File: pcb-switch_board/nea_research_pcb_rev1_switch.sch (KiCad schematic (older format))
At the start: 8 parts, among them P1 CONN_02X15, P2 CONN_02X13, P3 CONN_02X30, U1 QS4A110, U2 QS4A110, U3 QS4A110, U4 QS4A110, U5 QS4A110

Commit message: -progress on switch board layout
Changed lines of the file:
@@
 Text Label 1655 4540 0    60   ~ 0
 N2
-Text Label 1635 5300 0    60   ~ 0
+Text Label 1625 5460 0    60   ~ 0
 O2
-Text Label 1635 5460 0    60   ~ 0
+Text Label 1630 5300 0    60   ~ 0
 P2
 Text Label 1635 5660 0    60   ~ 0
@@
 Text Label 1605 6850 0    60   ~ 0
 U2
-Text Label 1590 7050 0    60   ~ 0
+Text Label 1610 7370 0    60   ~ 0
 V2
 Text Label 1570 1235 0    60   ~ 0
 MID2
-Text Label 1660 4100 0    60   ~ 0
+Text Label 1635 3780 0    60   ~ 0
 L1
 Text Label 1660 4300 0    60   ~ 0
@@
 Text Label 1655 4460 0    60   ~ 0
 N1
-Text Label 1640 5220 0    60   ~ 0
+Text Label 1630 5540 0    60   ~ 0
 O1
-Text Label 1640 5380 0    60   ~ 0
+Text Label 1630 5380 0    60   ~ 0
 P1
-Text Label 1640 5540 0    60   ~ 0
+Text Label 1625 5220 0    60   ~ 0
 Q1
 Text Label 1640 5740 0    60   ~ 0
@@
 Text Label 1610 6930 0    60   ~ 0
 V1
-Text Label 1545 7370 0    60   ~ 0
+Text Label 1530 7050 0    60   ~ 0
 SCL
+Text Label 1535 7130 0    60   ~ 0
+SDA
 Text Label 1535 7290 0    60   ~ 0
-SDA
-Text Label 1540 7130 0    60   ~ 0
 LED1
-Text Label 1520 7210 0    60   ~ 0
+Text Label 1535 7210 0    60   ~ 0
 LED2
 Text Label 1570 1155 0    60   ~ 0
@@
 Wire Wire Line
 	1895 1675 1570 1675
-Text Label 1680 2410 0    60   ~ 0
+Text Label 1615 2730 0    60   ~ 0
 E1
 Wire Wire Line
 	1865 2410 1540 2410
-Text Label 1680 2570 0    60   ~ 0
+Text Label 1605 2570 0    60   ~ 0
 F1
-Text Label 1680 2730 0    60   ~ 0
+Text Label 1600 2410 0    60   ~ 0
 G1
-Text Label 1680 2930 0    60   ~ 0
+Text Label 1610 3090 0    60   ~ 0
 H1
-Text Label 1680 3090 0    60   ~ 0
+Text Label 1610 2930 0    60   ~ 0
 I1
-Text Label 1660 3780 0    60   ~ 0
+Text Label 1640 4100 0    60   ~ 0
 J1
-Text Label 1660 3940 0    60   ~ 0
+Text Label 1640 3940 0    60   ~ 0
 K1
 Text Label 1570 1315 0    60   ~ 0
@@
 Text Label 1570 1435 0    60   ~ 0
 D2
-Text Label 1680 2490 0    60   ~ 0
+Text Label 1610 2650 0    60   ~ 0
 E2
-Text Label 1680 2650 0    60   ~ 0
+Text Label 1605 2490 0    60   ~ 0
 F2
-Text Label 1680 2850 0    60   ~ 0
+Text Label 1615 3170 0    60   ~ 0
 G2
-Text Label 1680 3010 0    60   ~ 0
+Text Label 1610 3010 0    60   ~ 0
 H2
-Text Label 1680 3170 0    60   ~ 0
+Text Label 1610 2850 0    60   ~ 0
 I2
-Text Label 1655 3860 0    60   ~ 0
+Text Label 1640 4020 0    60   ~ 0
 J2
-Text Label 1660 4020 0    60   ~ 0
+Text Label 1630 3860 0    60   ~ 0
 K2
 Wire Wire Line
@@
 Text Label 2800 4540 0    60   ~ 0
 N2_SW
-Text Label 2780 5300 0    60   ~ 0
+Text Label 2770 5460 0    60   ~ 0
 O2_SW
-Text Label 2780 5460 0    60   ~ 0
+Text Label 2770 5300 0    60   ~ 0
 P2_SW
 Text Label 2780 5660 0    60   ~ 0
@@
 Text Label 2750 6850 0    60   ~ 0
 U2_SW
-Text Label 2735 7050 0    60   ~ 0
+Text Label 2650 7370 0    60   ~ 0
 V2_SW
 Text Label 2785 1235 0    60   ~ 0
 MID2_SW
-Text Label 2805 4100 0    60   ~ 0
+Text Label 2695 3780 0    60   ~ 0
 L1_SW
 Text Label 2805 4300 0    60   ~ 0
@@
 Text Label 2800 4460 0    60   ~ 0
 N1_SW
-Text Label 2785 5220 0    60   ~ 0
+Text Label 2775 5540 0    60   ~ 0
 O1_SW
-Text Label 2785 5380 0    60   ~ 0
+Text Label 2770 5380 0    60   ~ 0
 P1_SW
-Text Label 2785 5540 0    60   ~ 0
+Text Label 2765 5220 0    60   ~ 0
 Q1_SW
 Text Label 2785 5740 0    60   ~ 0
@@
 Text Label 2755 6930 0    60   ~ 0
 V1_SW
-Text Label 2690 7370 0    60   ~ 0
+Text Label 2650 7050 0    60   ~ 0
 SCL_SW
-Text Label 2680 7290 0    60   ~ 0
+Text Label 2650 7130 0    60   ~ 0
 SDA_SW
-Text Label 2685 7130 0    60   ~ 0
+Text Label 2645 7290 0    60   ~ 0
 LED1_SW
-Text Label 2665 7210 0    60   ~ 0
+Text Label 2640 7210 0    60   ~ 0
 LED2_SW
 Wire Wire Line
@@
 Wire Wire Line
 	3040 1675 2715 1675
-Text Label 2825 2410 0    60   ~ 0
+Text Label 2735 2730 0    60   ~ 0
 E1_SW
 Wire Wire Line
 	3010 2410 2685 2410
-Text Label 2825 2570 0    60   ~ 0
+Text Label 2730 2570 0    60   ~ 0
 F1_SW
-Text Label 2825 2730 0    60   ~ 0
+Text Label 2730 2410 0    60   ~ 0
 G1_SW
-Text Label 2825 2930 0    60   ~ 0
+Text Label 2725 3090 0    60   ~ 0
 H1_SW
-Text Label 2825 3090 0    60   ~ 0
+Text Label 2720 2930 0    60   ~ 0
 I1_SW
-Text Label 2805 3780 0    60   ~ 0
+Text Label 2690 4100 0    60   ~ 0
 J1_SW
-Text Label 2805 3940 0    60   ~ 0
+Text Label 2700 3940 0    60   ~ 0
 K1_SW
 Text Label 2790 1315 0    60   ~ 0
@@
 Text Label 2790 1435 0    60   ~ 0
 D2_SW
-Text Label 2825 2490 0    60   ~ 0
+Text Label 2730 2650 0    60   ~ 0
 E2_SW
-Text Label 2825 2650 0    60   ~ 0
+Text Label 2730 2490 0    60   ~ 0
 F2_SW
-Text Label 2825 2850 0    60   ~ 0
+Text Label 2725 3170 0    60   ~ 0
 G2_SW
-Text Label 2825 3010 0    60   ~ 0
+Text Label 2720 3010 0    60   ~ 0
 H2_SW
-Text Label 2825 3170 0    60   ~ 0
+Text Label 2715 2850 0    60   ~ 0
 I2_SW
-Text Label 2800 3860 0    60   ~ 0
+Text Label 2695 4020 0    60   ~ 0
 J2_SW
-Text Label 2805 4020 0    60   ~ 0
+Text Label 2700 3860 0    60   ~ 0
 K2_SW
 Wire Wire Line

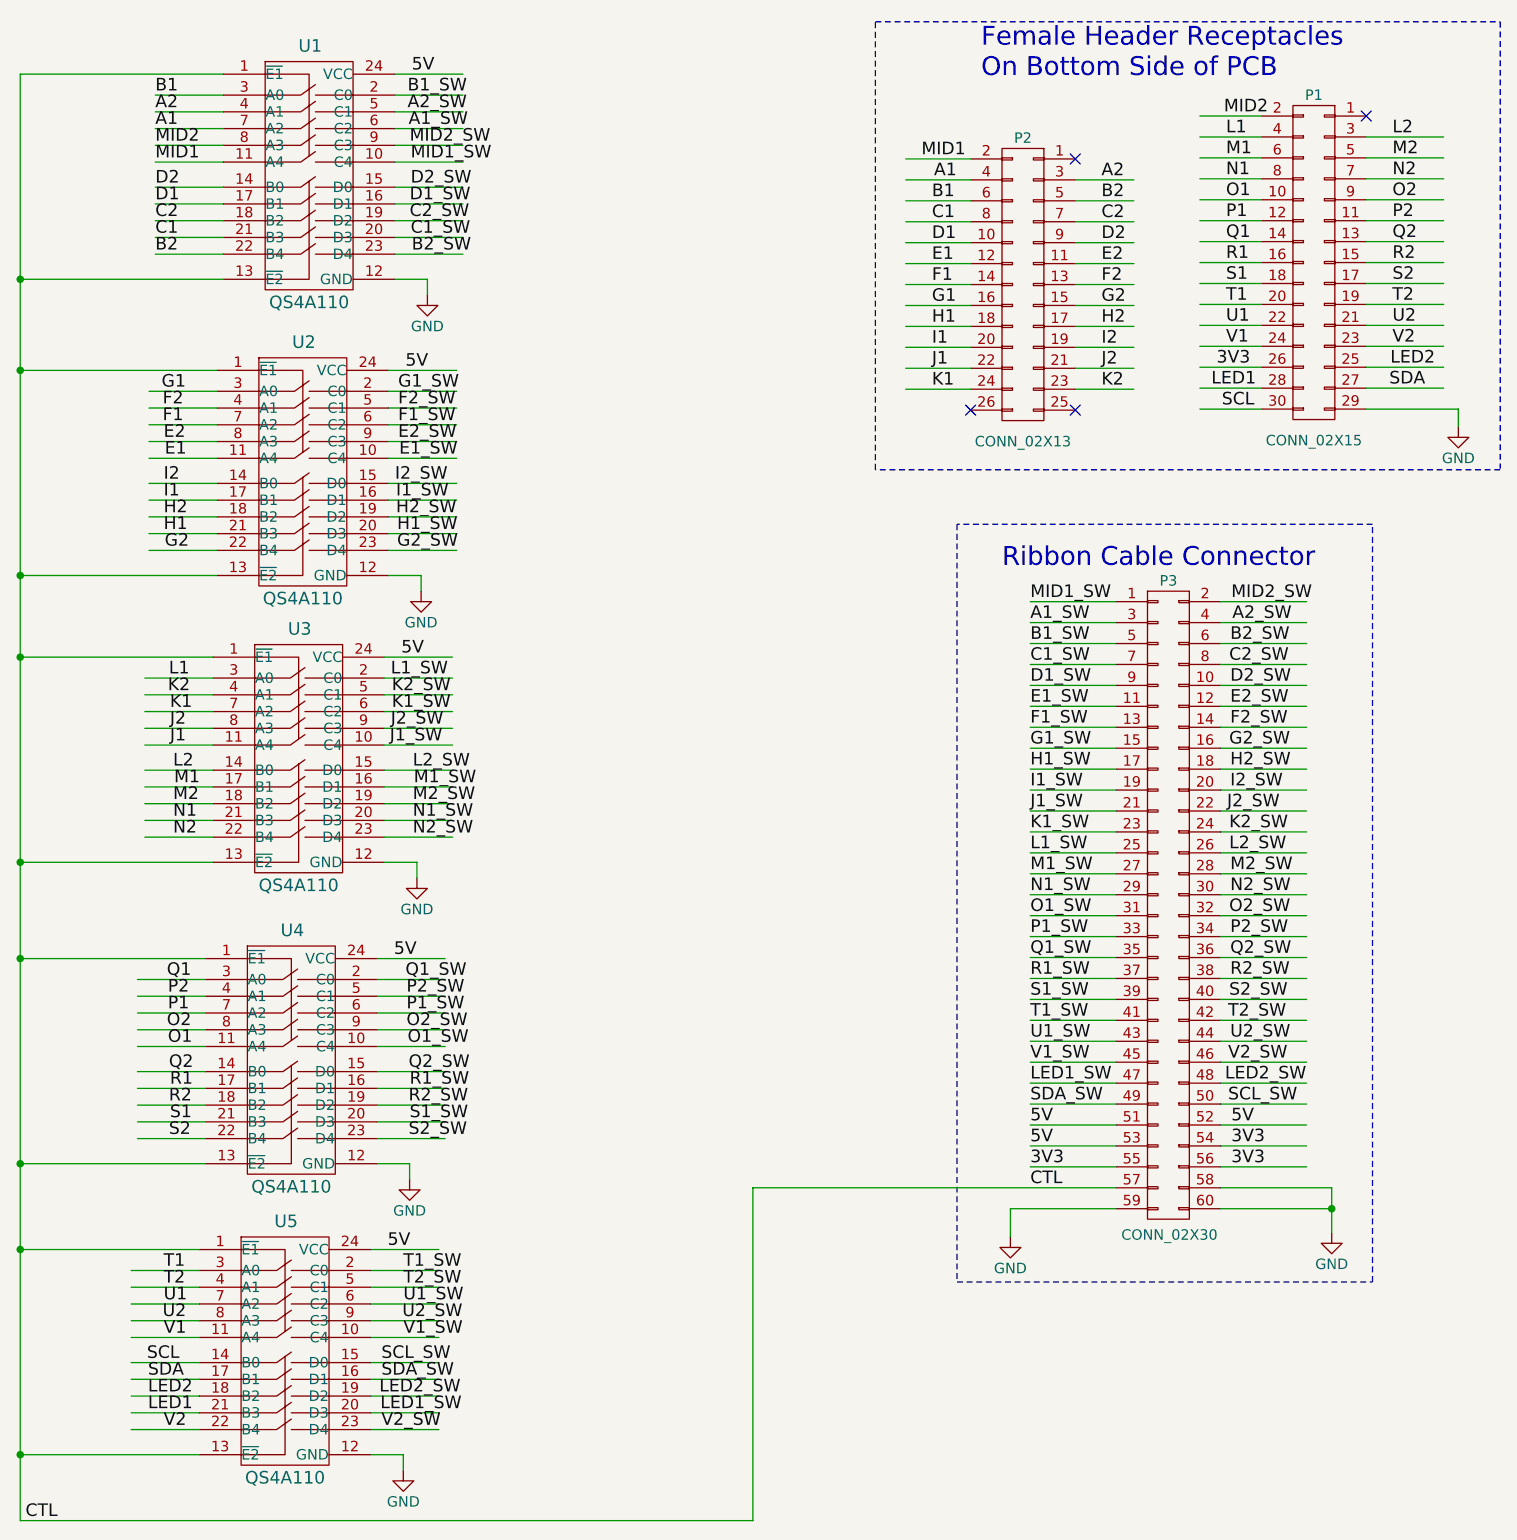
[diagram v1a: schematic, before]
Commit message: -finished rev1 of switch board layout -zip file sent off for pcb order
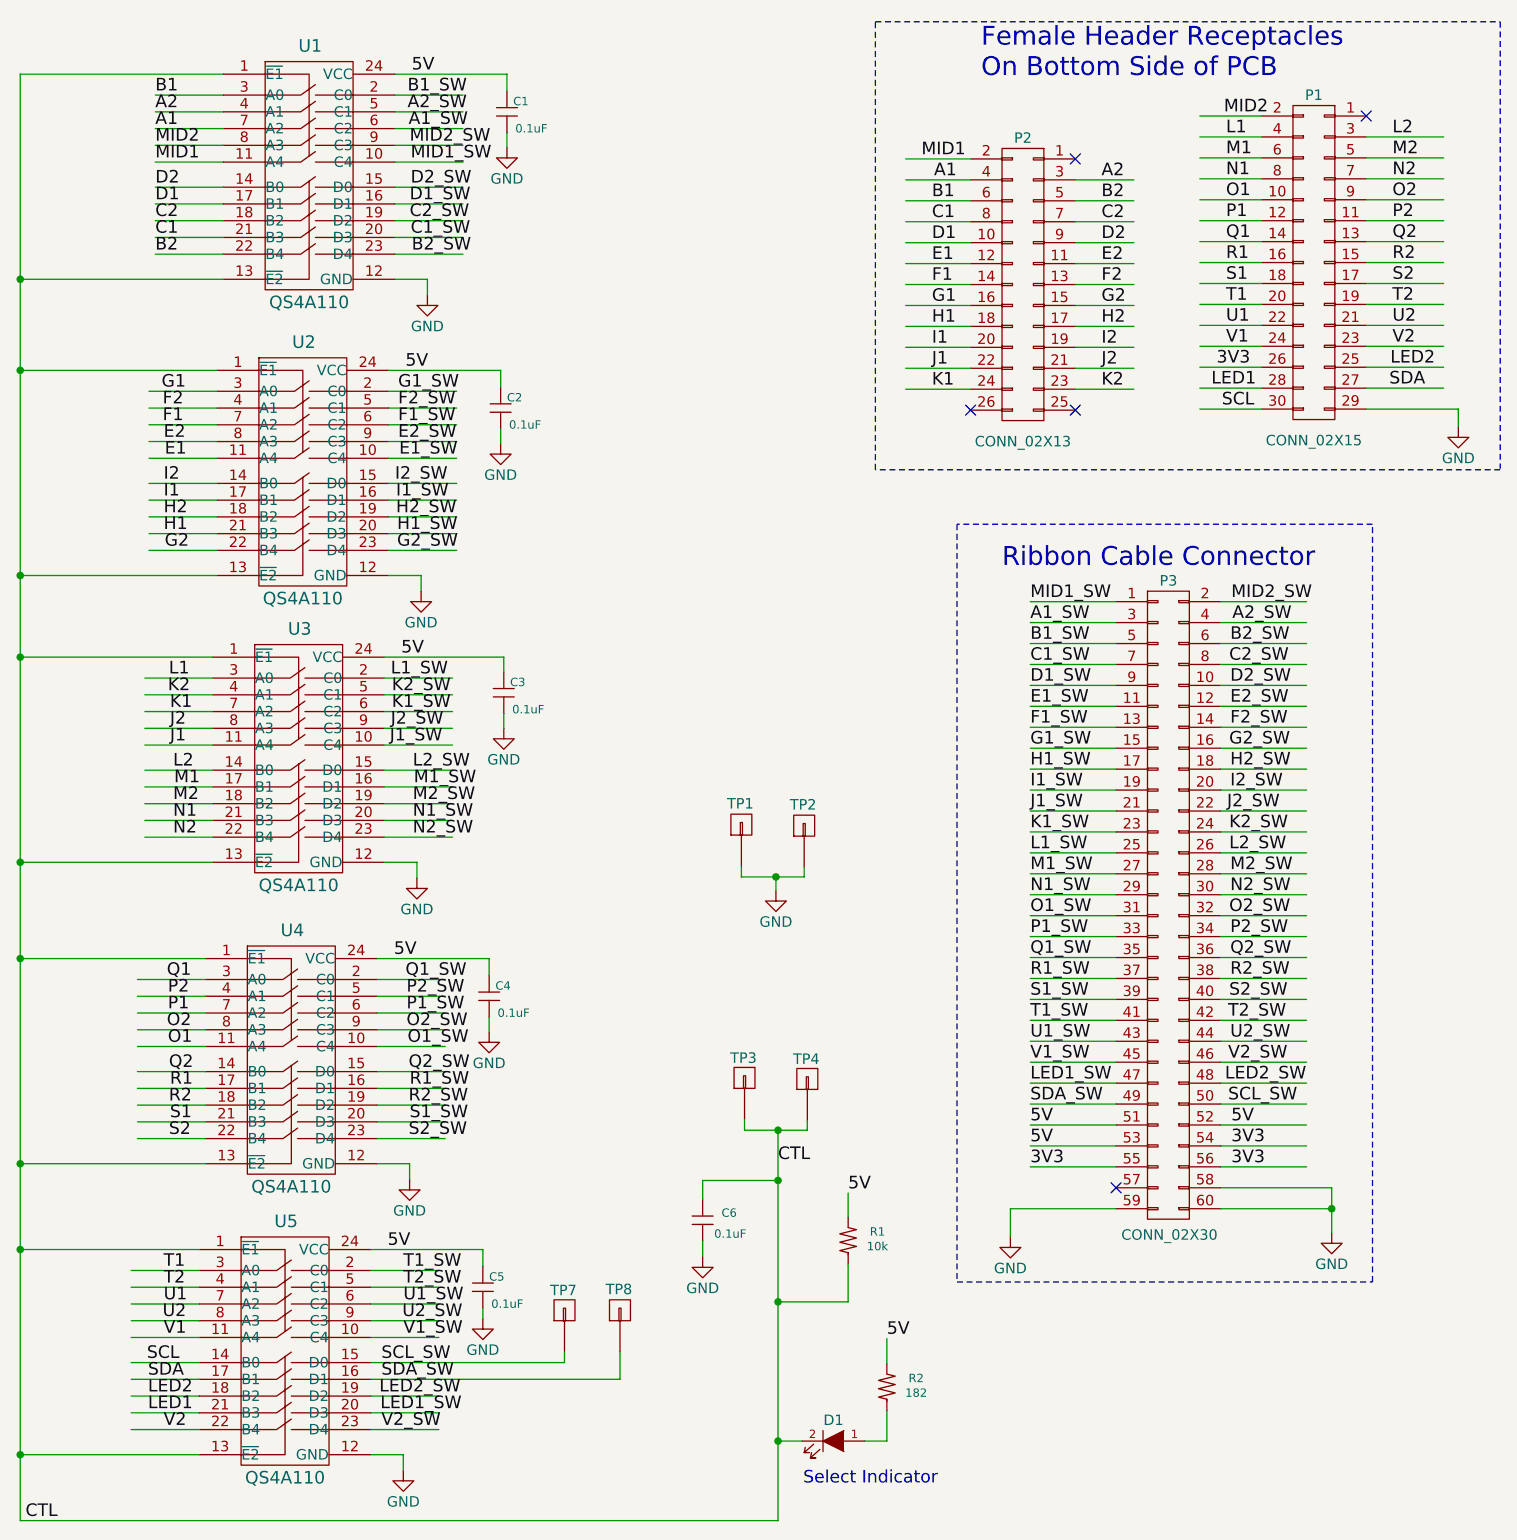
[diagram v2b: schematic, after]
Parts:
- added C1, C2, C3, C4, C5, C6: 0.1uF, footprints_on_Cdrive:0402, symbol CAP_NP
- added D1: LED_SMT, footprints:0603-D, symbol LED_SMT
- added R1: 10k, footprints_on_Cdrive:0603, symbol Res1_1
- added R2: 182, footprints_on_Cdrive:0603, symbol Res1_1
- added TP1, TP2, TP3, TP4, TP7, TP8: header_pin, footprints_on_Cdrive:Header_Pin_Rnd, symbol header_pin
- P1: footprint Pin_Headers:Pin_Header_Straight_2x15_Pitch2.54mm -> footprints_on_Cdrive:Pin_Header_Straight_2x15_Pitch2.54mm
- P2: footprint Pin_Headers:Pin_Header_Straight_2x13_Pitch2.54mm -> footprints_on_Cdrive:Pin_Header_Straight_2x13_Pitch2.54mm
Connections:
- wire segments 243 -> 271
- no-connect marks 4 -> 5
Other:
- note added: "Select Indicator"
